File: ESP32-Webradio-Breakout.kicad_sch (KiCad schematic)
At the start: 37 parts, among them J1 Conn_01x02, SW1 RotaryEncoder_Switch, U1 ESP32NodeMCU, U2 TSR_1-2450, U4 DS18B20

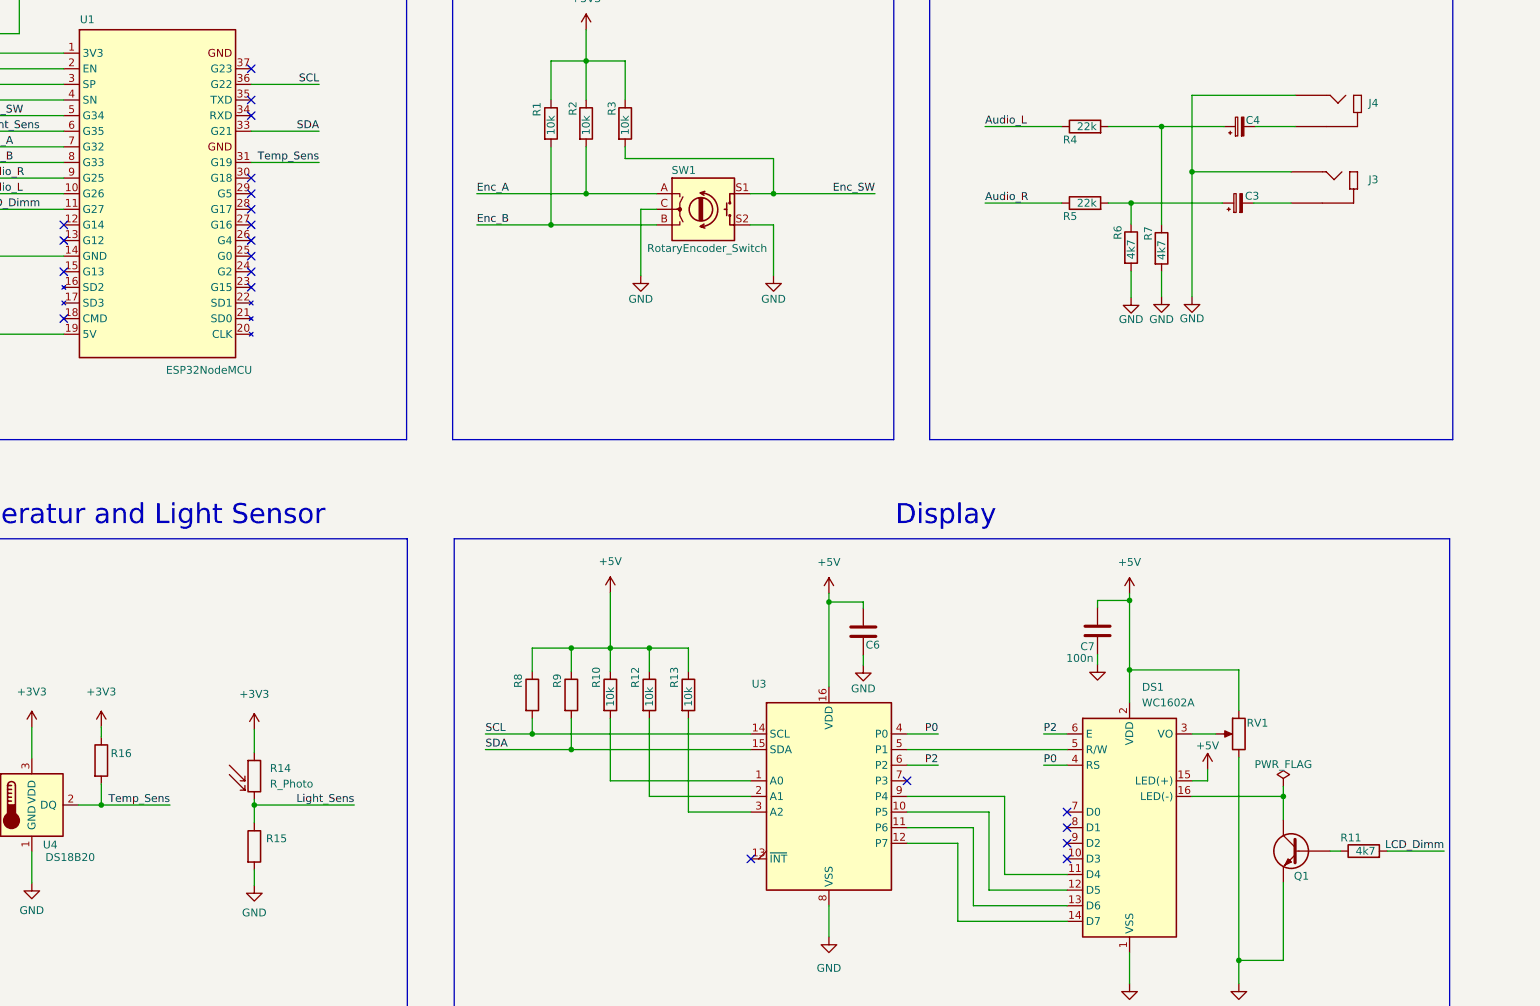
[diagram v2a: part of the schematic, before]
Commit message: Changed PCF8574A to PCF8574
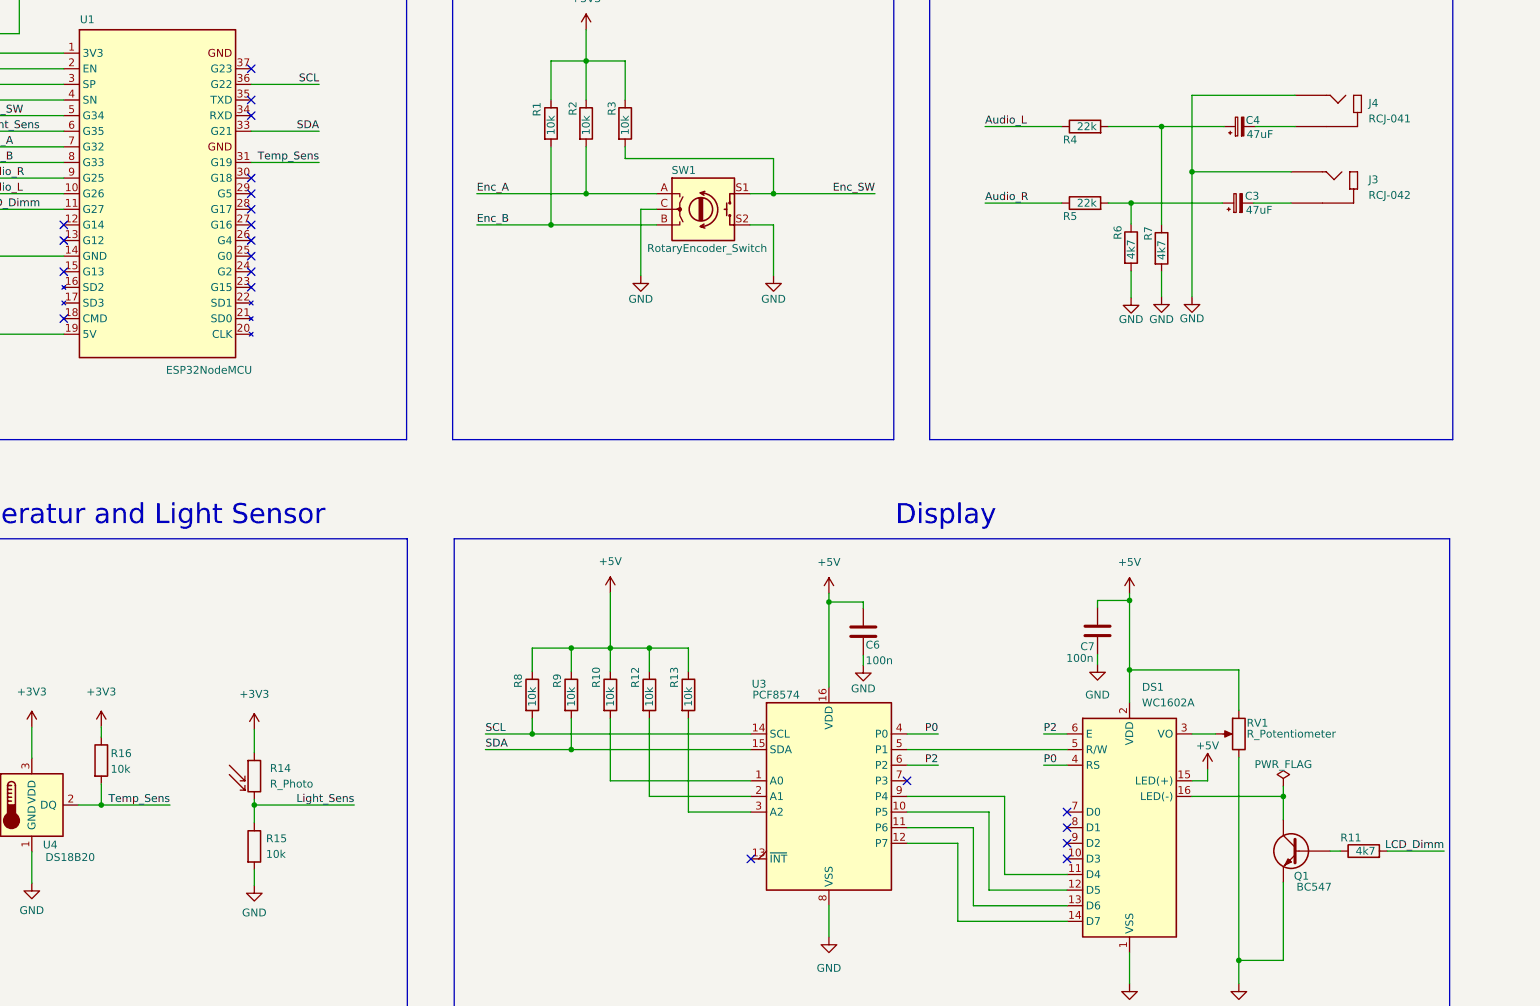
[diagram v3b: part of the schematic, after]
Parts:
- C3, C4: value (none) -> 47uF; footprint (none) -> Capacitor_THT:CP_Radial_D5.0mm_P2.50mm
- C5, C7: footprint (none) -> Capacitor_THT:C_Rect_L7.0mm_W3.5mm_P5.00mm
- C6: value (none) -> 100n; footprint (none) -> Capacitor_THT:C_Rect_L7.0mm_W3.5mm_P5.00mm
- J3: value (none) -> RCJ-042; footprint (none) -> RCJ-042:CUI_RCJ-042
- J4: value (none) -> RCJ-041; footprint (none) -> RCJ-041:CUI_RCJ-041
- Q1: value (none) -> BC547; footprint (none) -> Package_TO_SOT_THT:TO-92_Inline
- R15, R16, R8, R9: value (none) -> 10k
- RV1: value (none) -> R_Potentiometer; footprint (none) -> Potentiometer_THT:Potentiometer_ACP_CA9-V10_Vertical_Hole
- U3: value (none) -> PCF8574; footprint (none) -> Package_DIP:DIP-16_W10.16mm_LongPads
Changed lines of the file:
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@@
       (effects (font (size 1.27 1.27)) (justify left))
     )
-    (property "Footprint" "" (id 2) (at 337.3882 148.336 0)
+    (property "Footprint" "Capacitor_THT:C_Rect_L7.0mm_W3.5mm_P5.00mm" (id 2) (at 337.3882 148.336 0)
       (effects (font (size 1.27 1.27)) hide)
     )
@@
     (in_bom yes) (on_board yes)
     (property "Reference" "C4" (id 0) (at 361.696 61.468 90))
-    (property "Value" "" (id 1) (at 362.839 63.754 90))
-    (property "Footprint" "" (id 2) (at 359.537 62.484 0)
+    (property "Value" "47uF" (id 1) (at 362.839 63.754 90))
+    (property "Footprint" "Capacitor_THT:CP_Radial_D5.0mm_P2.50mm" (id 2) (at 359.537 62.484 0)
       (effects (font (size 1.27 1.27)) hide)
     )
@@
       (effects (font (size 1.27 1.27)) (justify left))
     )
-    (property "Value" "" (id 1) (at 201.168 180.8479 0)
+    (property "Value" "10k" (id 1) (at 201.168 180.8479 0)
       (effects (font (size 1.27 1.27)) (justify left))
     )
@@
       (effects (font (size 1.27 1.27)) (justify left))
     )
-    (property "Value" "" (id 1) (at 280.289 154.94 0)
-      (effects (font (size 1.27 1.27)) (justify left))
-    )
-    (property "Footprint" "" (id 2) (at 292.735 171.45 0)
+    (property "Value" "PCF8574" (id 1) (at 280.289 154.94 0)
+      (effects (font (size 1.27 1.27)) (justify left))
+    )
+    (property "Footprint" "Package_DIP:DIP-16_W10.16mm_LongPads" (id 2) (at 292.735 171.45 0)
       (effects (font (size 1.27 1.27)) hide)
     )
@@
       (effects (font (size 1.27 1.27)) (justify left))
     )
-    (property "Value" "" (id 1) (at 175.895 167.005 0)
+    (property "Value" "10k" (id 1) (at 175.895 167.005 0)
       (effects (font (size 1.27 1.27)) (justify left))
     )
@@
       (effects (font (size 1.27 1.27)) (justify left))
     )
-    (property "Footprint" "" (id 2) (at 151.9682 176.022 0)
+    (property "Footprint" "Capacitor_THT:C_Rect_L7.0mm_W3.5mm_P5.00mm" (id 2) (at 151.9682 176.022 0)
       (effects (font (size 1.27 1.27)) hide)
     )
@@
       (effects (font (size 1.27 1.27)) hide)
     )
-    (property "Value" "" (id 1) (at 336.423 154.94 0))
+    (property "Value" "GND" (id 1) (at 336.423 154.94 0))
     (property "Footprint" "" (id 2) (at 336.423 149.987 0)
       (effects (font (size 1.27 1.27)) hide)
@@
       (effects (font (size 1.27 1.27)) (justify right))
     )
-    (property "Value" "" (id 1) (at 380.492 61.2139 0)
+    (property "Value" "RCJ-041" (id 1) (at 380.492 61.2139 0)
       (effects (font (size 1.27 1.27)) (justify right))
     )
-    (property "Footprint" "" (id 2) (at 373.634 59.944 0)
+    (property "Footprint" "RCJ-041:CUI_RCJ-041" (id 2) (at 373.634 59.944 0)
       (effects (font (size 1.27 1.27)) (justify left bottom) hide)
     )
@@
       (effects (font (size 1.27 1.27)) (justify right))
     )
-    (property "Value" "" (id 1) (at 360.68 161.29 0)
+    (property "Value" "R_Potentiometer" (id 1) (at 360.68 161.29 0)
       (effects (font (size 1.27 1.27)) (justify right))
     )
-    (property "Footprint" "" (id 2) (at 359.41 161.29 0)
+    (property "Footprint" "Potentiometer_THT:Potentiometer_ACP_CA9-V10_Vertical_Hole" (id 2) (at 359.41 161.29 0)
       (effects (font (size 1.27 1.27)) hide)
     )
@@
       (effects (font (size 1.27 1.27)) (justify left))
     )
-    (property "Value" "" (id 1) (at 374.523 186.182 0)
-      (effects (font (size 1.27 1.27)) (justify left))
-    )
-    (property "Footprint" "" (id 2) (at 364.109 182.245 0)
+    (property "Value" "BC547" (id 1) (at 374.523 186.182 0)
+      (effects (font (size 1.27 1.27)) (justify left))
+    )
+    (property "Footprint" "Package_TO_SOT_THT:TO-92_Inline" (id 2) (at 364.109 182.245 0)
       (effects (font (size 1.27 1.27) italic) (justify left) hide)
     )
@@
       (effects (font (size 1.27 1.27)) (justify left))
     )
-    (property "Value" "" (id 1) (at 244.475 156.845 90)
+    (property "Value" "10k" (id 1) (at 244.475 156.845 90)
       (effects (font (size 1.27 1.27)) (justify left))
     )
@@
       (effects (font (size 1.27 1.27)) (justify left))
     )
-    (property "Value" "" (id 1) (at 250.825 156.845 90)
+    (property "Value" "10k" (id 1) (at 250.825 156.845 90)
       (effects (font (size 1.27 1.27)) (justify left))
     )
@@
       (effects (font (size 1.27 1.27)) (justify left))
     )
-    (property "Value" "" (id 1) (at 298.704 149.352 0)
-      (effects (font (size 1.27 1.27)) (justify left))
-    )
-    (property "Footprint" "" (id 2) (at 299.2882 148.463 0)
+    (property "Value" "100n" (id 1) (at 298.704 149.352 0)
+      (effects (font (size 1.27 1.27)) (justify left))
+    )
+    (property "Footprint" "Capacitor_THT:C_Rect_L7.0mm_W3.5mm_P5.00mm" (id 2) (at 299.2882 148.463 0)
       (effects (font (size 1.27 1.27)) hide)
     )
@@
     (in_bom yes) (on_board yes)
     (property "Reference" "C3" (id 0) (at 361.569 73.787 90))
-    (property "Value" "" (id 1) (at 362.712 76.073 90))
-    (property "Footprint" "" (id 2) (at 359.283 74.93 0)
+    (property "Value" "47uF" (id 1) (at 362.712 76.073 90))
+    (property "Footprint" "Capacitor_THT:CP_Radial_D5.0mm_P2.50mm" (id 2) (at 359.283 74.93 0)
       (effects (font (size 1.27 1.27)) hide)
     )
@@
       (effects (font (size 1.27 1.27)) (justify right))
     )
-    (property "Value" "" (id 1) (at 380.492 73.6599 0)
+    (property "Value" "RCJ-042" (id 1) (at 380.492 73.6599 0)
       (effects (font (size 1.27 1.27)) (justify right))
     )
-    (property "Footprint" "" (id 2) (at 372.999 72.39 0)
+    (property "Footprint" "RCJ-042:CUI_RCJ-042" (id 2) (at 372.999 72.39 0)
       (effects (font (size 1.27 1.27)) (justify left bottom) hide)
     )
@@
     )
     (path "/407d0cd8-54f8-47a8-90cb-42c8a441d04f"
-      (reference "U3") (unit 1) (value "PCF8574A") (footprint "Package_DIP:DIP-16_W10.16mm_LongPads")
+      (reference "U3") (unit 1) (value "PCF8574") (footprint "Package_DIP:DIP-16_W10.16mm_LongPads")
     )
     (path "/a6b82443-9372-497e-a356-3173065d1b81"

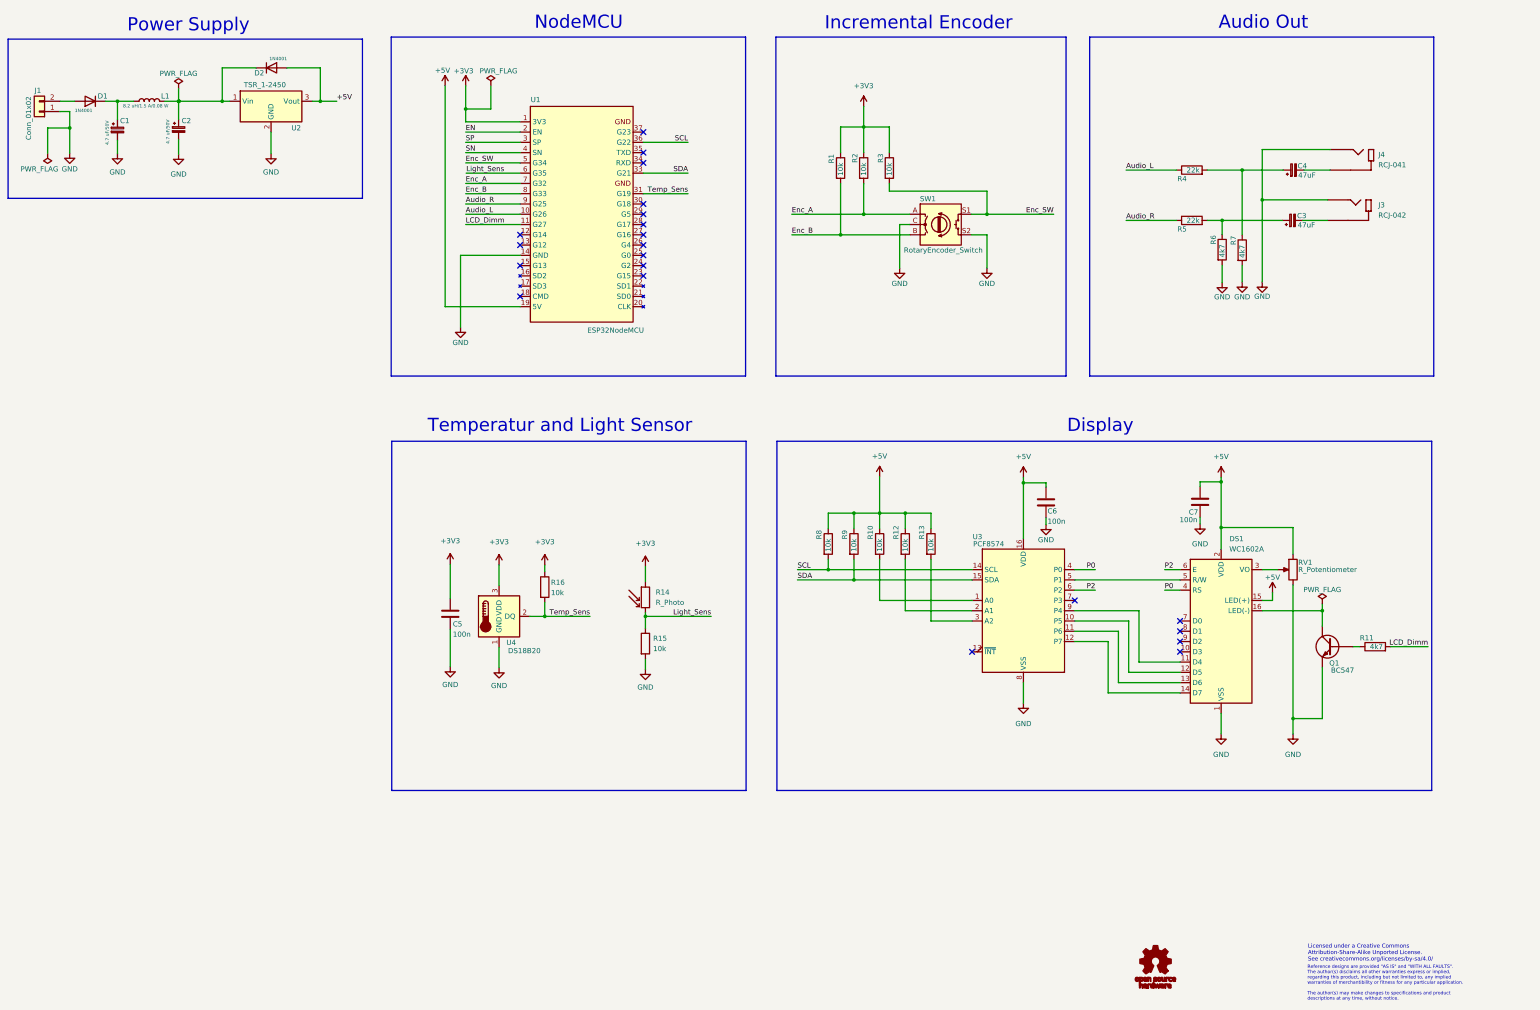
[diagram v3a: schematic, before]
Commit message: Added solder pads for I2C display
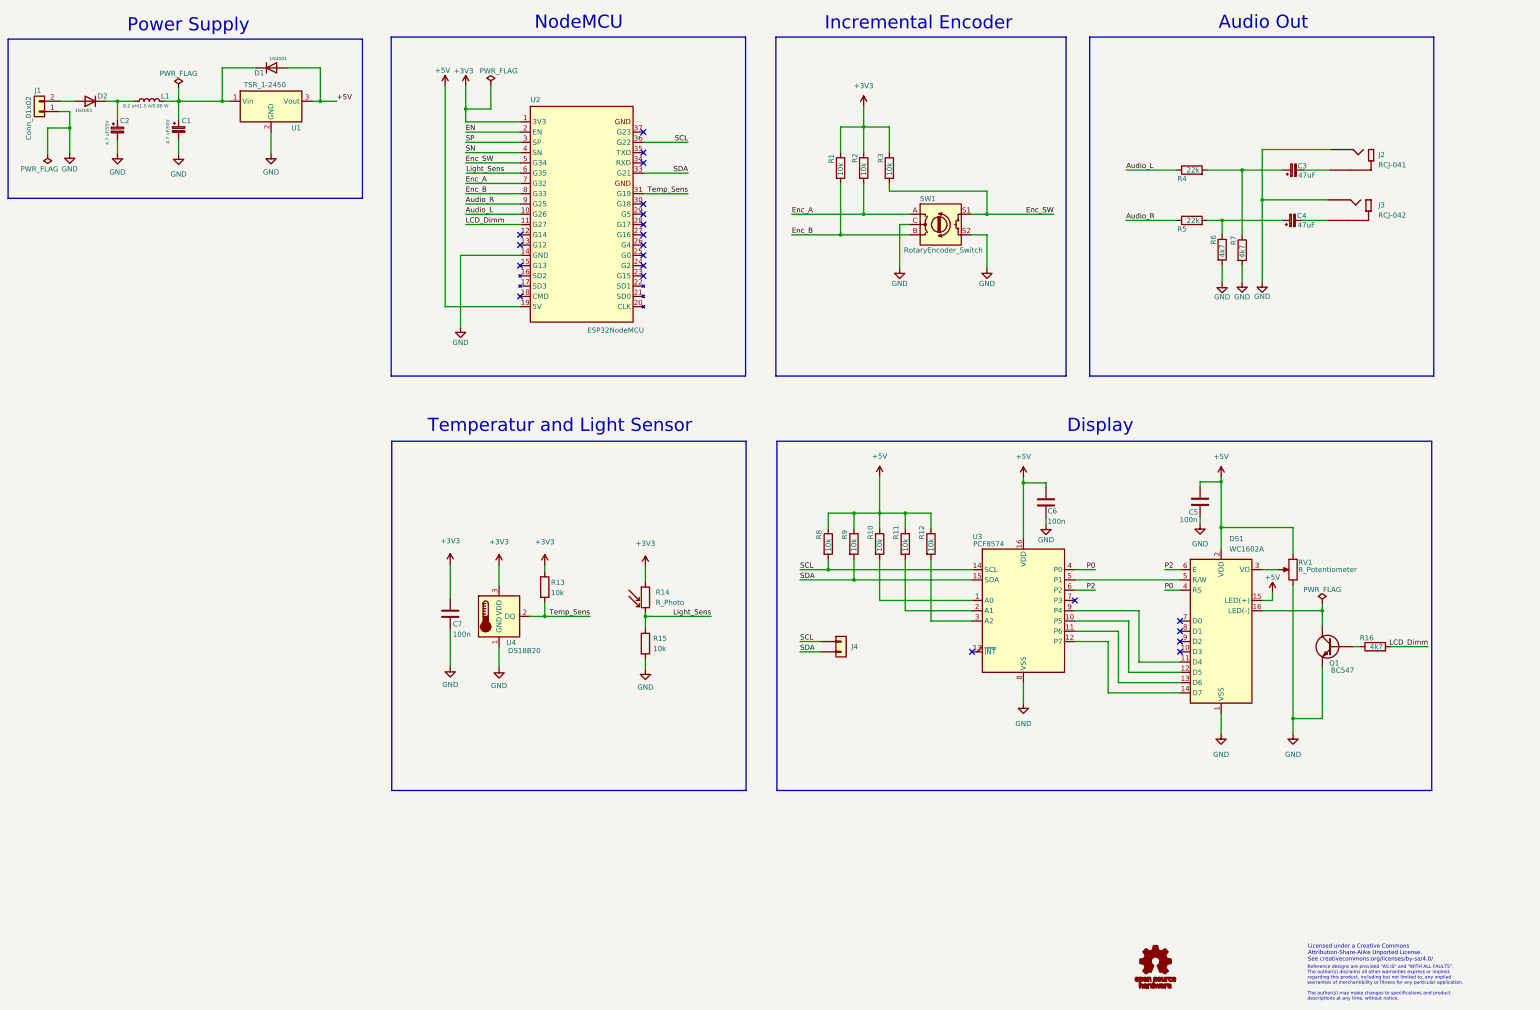
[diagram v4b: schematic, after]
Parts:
- added J4: Conn_01x02, TestPoint:TestPoint_2Pads_Pitch2.54mm_Drill0.8mm, symbol Connector_Generic:Conn_01x02
- renumbered C2 to C1, C1 to C2, C4 to C3, C3 to C4, C7 to C5, C5 to C7, D2 to D1, D1 to D2, J4 to J2, R12 to R11, R13 to R12, R16 to R13, R11 to R16, U2 to U1, U1 to U2
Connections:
- net SCL: now also J4.1 (Pin_1)
- net SDA: now also J4.2 (Pin_2)
